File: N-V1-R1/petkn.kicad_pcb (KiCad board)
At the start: 2 copper layers, 386.1 x 99.6 mm, 83 parts, among them J1 Conn_01x20, J2 Conn_02x03_Odd_Even, J3 LINK3, J4 Conn_01x20, J5 SPACE1, J6 SPACE2, J67 LINK67, SW1 KP "=", SW10 KP "0", SW11 R SHIFT, SW12 ">", SW14 "]", SW15 "@", SW16 L SHIFT, SW17 KP "+", SW18 KP "2", SW2 KP ".", SW20 "?", SW21 ",", SW22 "N", SW23 "V", SW24 "X", SW25 KP "3", SW26 KP "1", SW27 RETURN, SW28 ";", SW29 "M", SW3 NC ($10), SW30 "B", SW31 "C", SW32 "Z", SW320 S LOCK, SW33 KP "*", SW34 KP "5", SW36 ":", SW37 "K", SW38 "H", SW39 "F", SW4 STOP, SW40 "S", SW41 KP "6", SW42 KP "4", SW44 "L", SW45 "J", SW46 "G", SW47 "D", SW48 "A", SW49 KP "/", SW5 "<", SW50 KP "8", SW52 "P", SW53 "I", SW54 "Y", SW55 "R", SW56 "W", SW57 KP "9", SW58 KP "7", SW59 U ARROW, SW6 SPACE, SW60 "O", SW61 "U", SW62 "T", SW63 "E", SW64 "Q", SW65 INS/DEL, SW66 UP/DOWN, SW67 NC ($0A), SW68 ")", SW69 "\", SW7 "[", SW70 "'", SW71 "$", SW72 QUOTE, SW73 LEFT/RIGHT, SW74 CLR/HOME, SW75 B ARROW, SW76 "(", SW77 "&", SW78 "%", SW79 "#"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

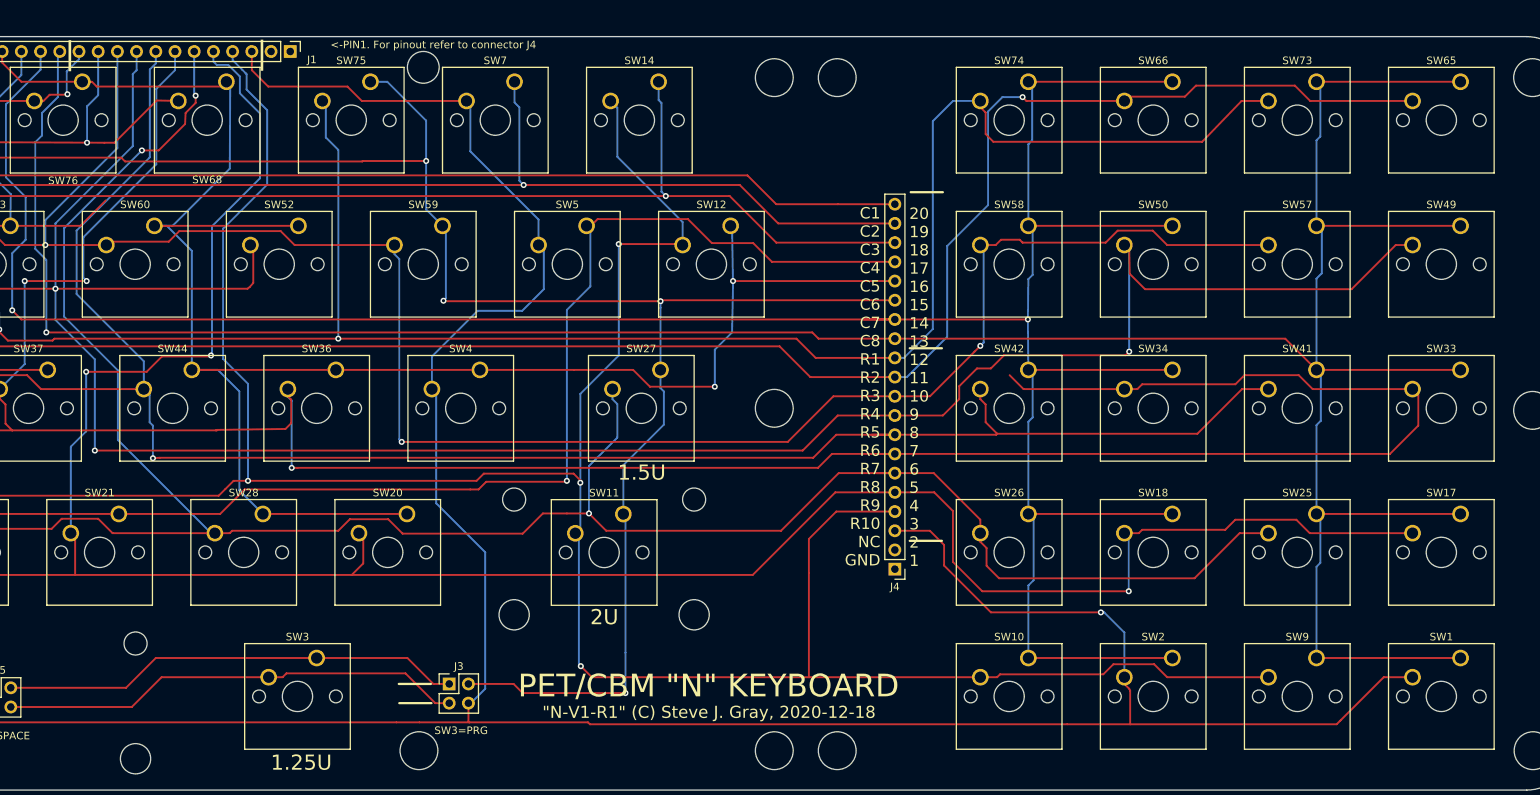
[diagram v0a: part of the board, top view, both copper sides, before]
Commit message: N-V1-R1 spacing fix.
Gerber directory renamed. Do not use gerbers! Fix to PCB  spacing.
Should be ok, but no gerbers or pcb yet. use at own risk! Do not use the
gerbers in the error directory unless you just need a keyboard and wont
be installing it in a case!
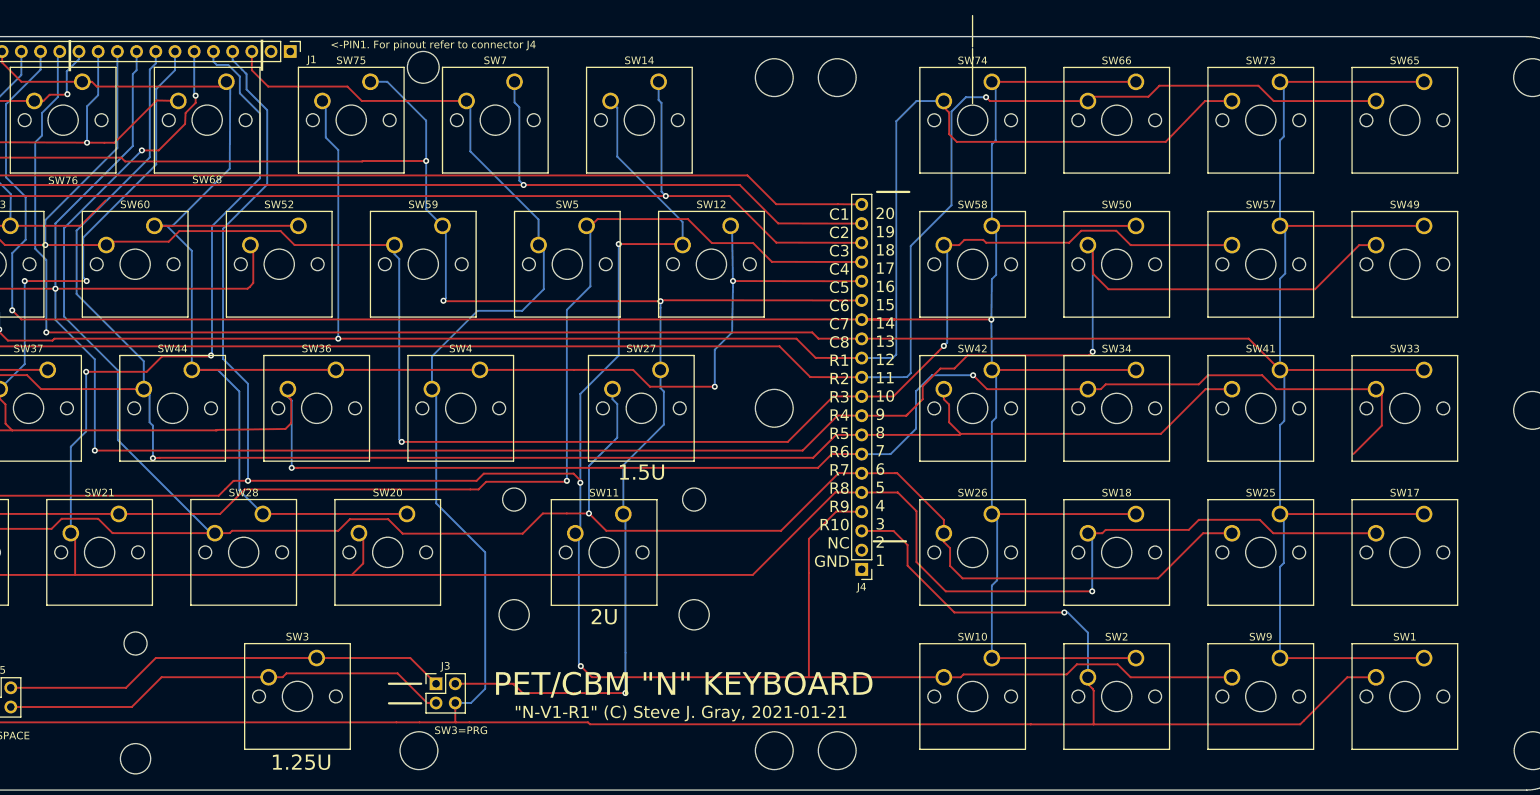
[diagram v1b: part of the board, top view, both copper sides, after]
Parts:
- moved SW1 4.83 mm to (383.9, 130.8)
- moved SW17 4.83 mm to (383.9, 111.7)
- moved SW25 4.83 mm to (364.9, 111.7)
- moved SW33 4.83 mm to (383.9, 92.7)
- moved SW41 4.83 mm to (364.9, 92.7)
- moved SW49 4.83 mm to (383.9, 73.6)
- moved SW57 4.83 mm to (364.9, 73.6)
- moved SW65 4.83 mm to (383.9, 54.6)
- moved SW73 4.83 mm to (364.9, 54.6)
- moved SW9 4.83 mm to (364.9, 130.8)
- moved SW10 4.83 mm to (326.8, 130.8)
- moved SW18 4.83 mm to (345.8, 111.7)
- moved SW2 4.83 mm to (345.8, 130.8)
- moved SW26 4.83 mm to (326.8, 111.7)
- moved SW34 4.83 mm to (345.8, 92.7)
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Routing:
- net R6: track 465.1 -> 414.2 mm, vias 3 -> 4
- net R9: track 599.2 -> 590.0 mm
- net R5: track 382.0 -> 374.0 mm
- net R7: track 417.5 -> 410.3 mm
- net C7: track 350.4 -> 345.6 mm
- net C8: track 382.4 -> 377.6 mm
- net R3: track 389.6 -> 384.7 mm
- net R8: track 435.1 -> 430.2 mm
- net R4: track 536.8 -> 532.2 mm
- net C5: track 256.4 -> 252.0 mm
- net C4: track 309.2 -> 304.8 mm
- net C3: track 442.0 -> 437.6 mm
- net C2: track 513.9 -> 509.5 mm
- net C1: track 514.0 -> 509.6 mm
- net R10: track 644.5 -> 641.0 mm
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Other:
- board text added: ""N-V1-R1" (C) Steve J. Gray, 2021-01-21"
- board text removed: ""N-V1-R1" (C) Steve J. Gray, 2020-12-18"
